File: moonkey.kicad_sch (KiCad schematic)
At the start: 35 parts, among them SW1 SW_Push, SW10 SW_Push, SW11 SW_Push, SW12 SW_Push, SW13 SW_Push, SW14 SW_Push, SW15 SW_Push, SW16 SW_Push, SW17 SW_Push, SW2 SW_Push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

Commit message: update
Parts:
- added J1: AudioJack4, moonkey:PJ320A, symbol Connector:AudioJack4
- RZ1: renamed from RZ?; footprint (none) -> moonkey:RP2040
- SW1, SW10, SW11, SW12, SW13, SW14, SW15, SW16, SW17, SW2, SW3, SW4, SW5, SW6, SW7, SW8, SW9: footprint Switch_Keyboard_Cherry_MX:SW_Cherry_MX_PCB_1.00u -> moonkey:Cherry_1u_rev
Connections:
- net COL0: now reaches D1.1 (K), D10.1 (K), D14.1 (K), D4.1 (K)
- net COL0: now also D7.1 (K), RZ1.17 (GP26)
- net ROW4: now reaches SW14.2, SW15.2, SW16.2, SW17.2
- net ROW4: now also RZ1.8 (GP7)
- net COL2: now reaches D12.1 (K), D16.1 (K), D3.1 (K), D6.1 (K), D9.1 (K)
- net COL2: now also RZ1.19 (GP28)
- net ROW0: now reaches SW1.2, SW2.2, SW3.2
- net ROW0: now also RZ1.1 (GP0)
- net ROW2: now reaches SW7.2, SW8.2, SW9.2
- net ROW2: now also RZ1.7 (GP6)
- net COL1: now reaches RZ1.18 (GP27)
- net COL1: now also D11.1 (K), D15.1 (K), D2.1 (K), D5.1 (K), D8.1 (K)
- net ROW1: now reaches RZ1.2 (GP1)
- net ROW1: now also SW4.2, SW5.2, SW6.2
- net COL3: now reaches RZ1.20 (GP29)
- net COL3: now also D13.1 (K), D17.1 (K)
- net +5V: now reaches RZ1.22 (5V)
- net +5V: now also J1.S
- net Earth: now reaches RZ1.23 (GND)
- net Earth: now also J1.T
- net SPI0_TX: now reaches RZ1.4 (GP3)
- net SPI0_TX: now also J1.R1
- net SPI0_RX: now reaches RZ1.5 (GP4)
- net SPI0_RX: now also J1.R2
- net ROW3: now reaches RZ1.9 (GP8)
- net ROW3: now also SW10.2, SW11.2, SW12.2, SW13.2
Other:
- moved on the sheet: D1, D10, D11, D12, D13, D14, D15, D16, D17, D2, D3, D4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

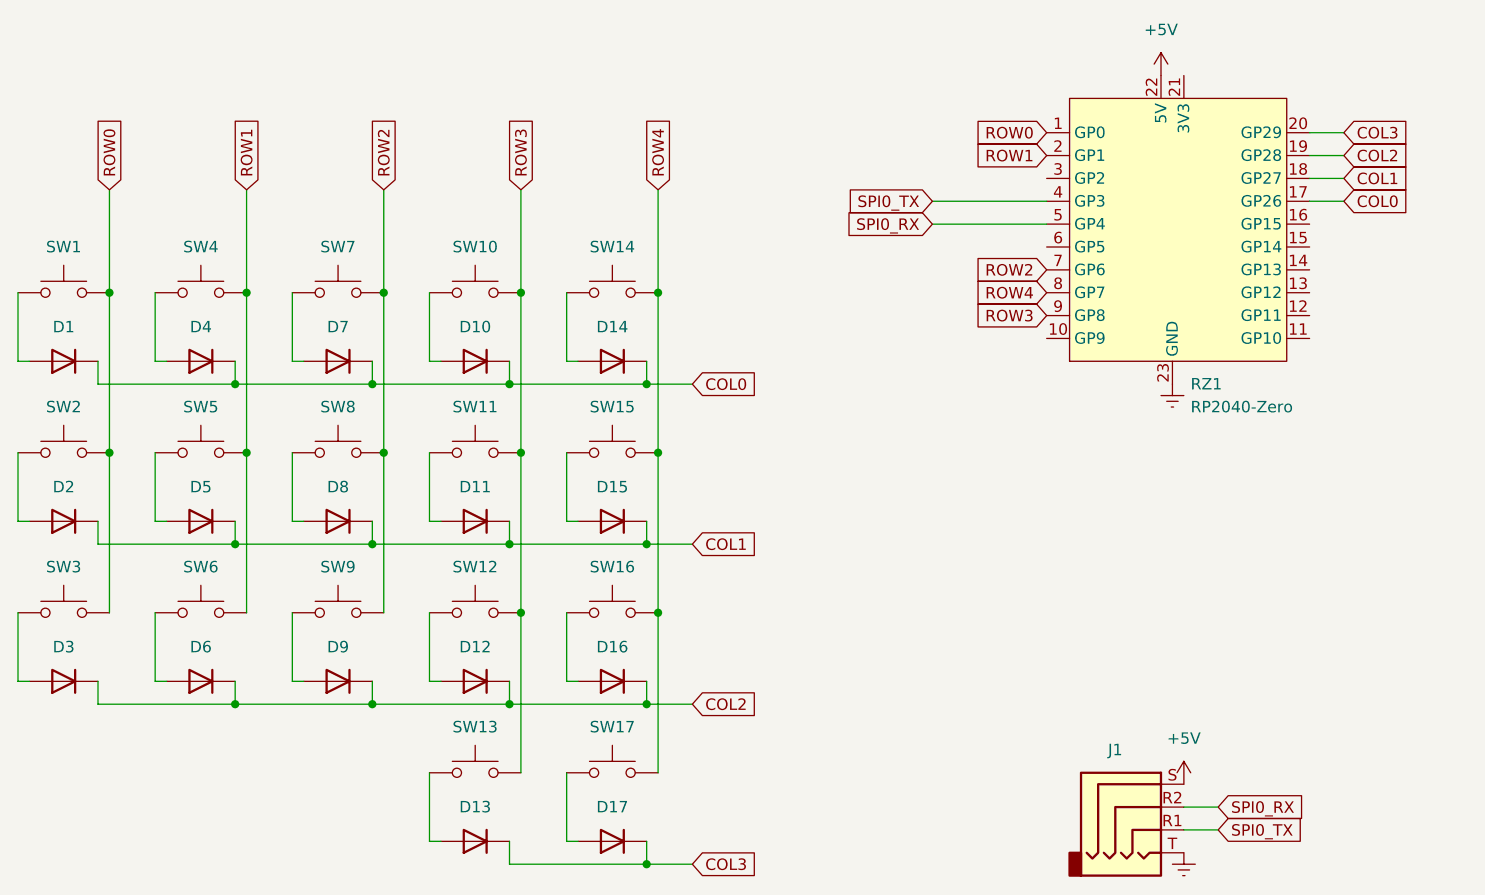
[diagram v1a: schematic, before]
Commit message: keyboard layout chagned, scheme update(pins change)
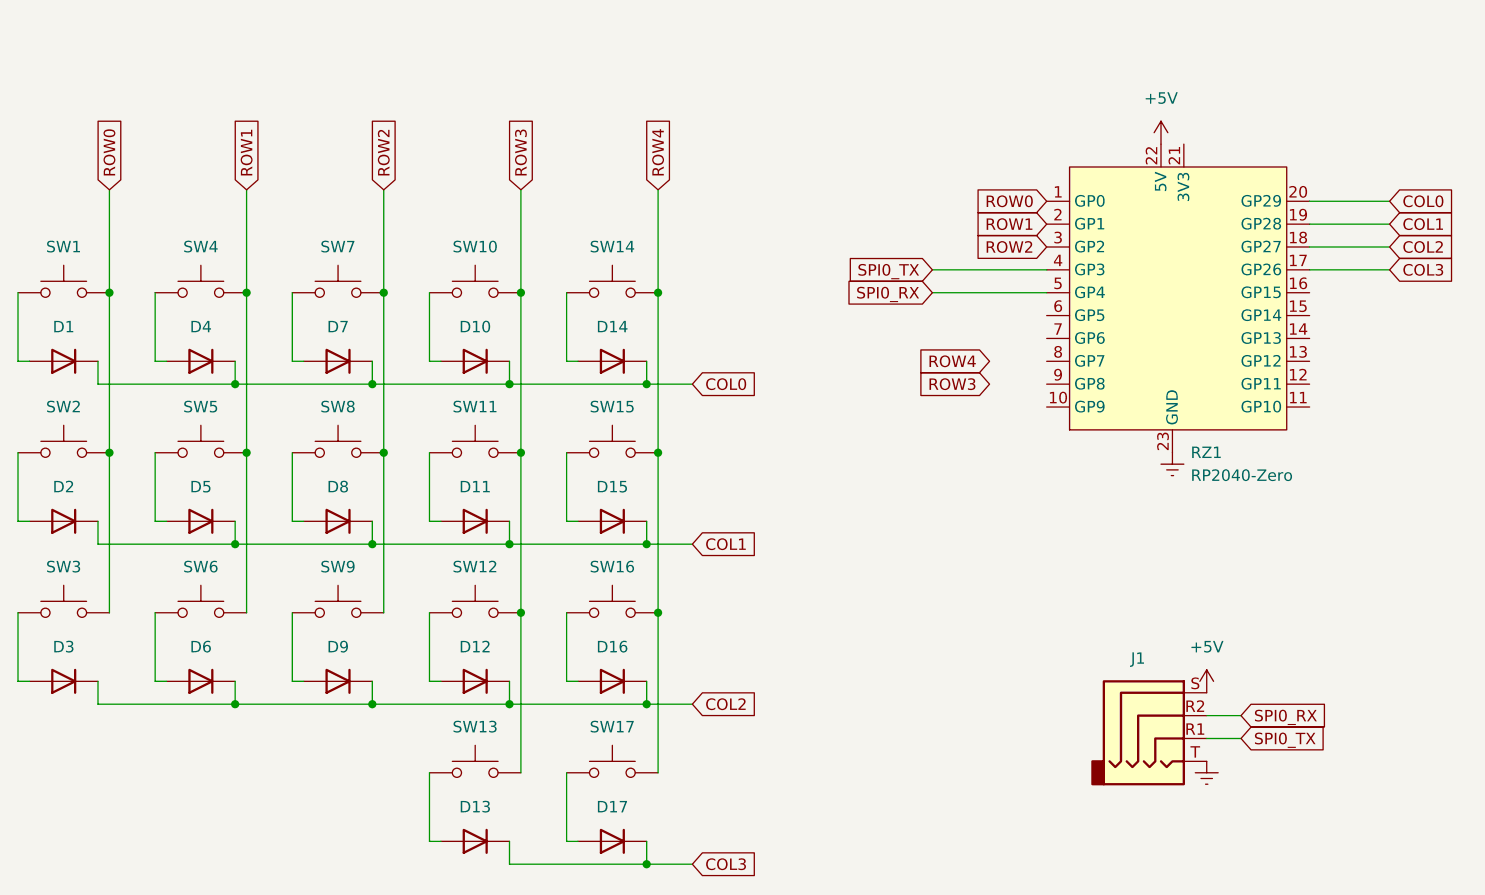
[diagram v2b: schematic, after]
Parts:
- J1: footprint moonkey:PJ320A -> moonkey:PJ320D_rev
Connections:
- net COL0: now also RZ1.20 (GP29); no longer RZ1.17 (GP26)
- net COL1: now also RZ1.19 (GP28); no longer RZ1.18 (GP27)
- net COL2: now also RZ1.18 (GP27); no longer RZ1.19 (GP28)
- net COL3: now also RZ1.17 (GP26); no longer RZ1.20 (GP29)
- net ROW2: now also RZ1.3 (GP2); no longer RZ1.7 (GP6)
- net ROW3: no longer RZ1.9 (GP8)
- net ROW4: no longer RZ1.8 (GP7)
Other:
- moved on the sheet: J1, RZ1

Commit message: uptate: ortholinear
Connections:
- net ROW3: now also RZ1.7 (GP6)
- net ROW4: now also RZ1.8 (GP7)
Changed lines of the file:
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@@
+    (stroke (width 0) (type default) (color 0 0 0 0))
+  )
+  (wire (pts (xy 151.13 86.36) (xy 153.67 86.36))
     (stroke (width 0) (type default) (color 0 0 0 0))
   )
@@
     (stroke (width 0) (type default) (color 0 0 0 0))
   )
+  (wire (pts (xy 151.13 71.12) (xy 153.67 71.12))
+    (stroke (width 0) (type default) (color 0 0 0 0))
+  )
   (wire (pts (xy 54.61 106.68) (xy 55.88 106.68))
     (stroke (width 0) (type default) (color 0 0 0 0))
@@
     (stroke (width 0) (type default) (color 0 0 0 0))
   )
+  (wire (pts (xy 151.13 73.66) (xy 153.67 73.66))
+    (stroke (width 0) (type default) (color 0 0 0 0))
+  )
   (wire (pts (xy 54.61 81.28) (xy 54.61 88.9))
     (stroke (width 0) (type default) (color 0 0 0 0))
@@
     (stroke (width 0) (type default) (color 0 0 0 0))
   )
+  (wire (pts (xy 151.13 88.9) (xy 153.67 88.9))
+    (stroke (width 0) (type default) (color 0 0 0 0))
+  )
   (wire (pts (xy 48.26 124.46) (xy 48.26 127))
     (stroke (width 0) (type default) (color 0 0 0 0))
@@
     (stroke (width 0) (type default) (color 0 0 0 0))
   )
+  (wire (pts (xy 151.13 76.2) (xy 153.67 76.2))
+    (stroke (width 0) (type default) (color 0 0 0 0))
+  )
   (wire (pts (xy 109.22 127) (xy 114.3 127))
     (stroke (width 0) (type default) (color 0 0 0 0))
@@
     )
   )
-  (global_label "ROW0" (shape input) (at 153.67 71.12 180) (fields_autoplaced)
-    (effects (font (size 1.27 1.27)) (justify right))
-    (property "시트 간 참조" "${INTERSHEET_REFS}" (id 0) (at 145.9955 71.0406 0)
+  (global_label "ROW0" (shape input) (at 151.13 71.12 180) (fields_autoplaced)
+    (effects (font (size 1.27 1.27)) (justify right))
+    (property "시트 간 참조" "${INTERSHEET_REFS}" (id 0) (at 143.4555 71.0406 0)
       (effects (font (size 1.27 1.27)) (justify right) hide)
     )
@@
     )
   )
-  (global_label "ROW1" (shape input) (at 153.67 73.66 180) (fields_autoplaced)
-    (effects (font (size 1.27 1.27)) (justify right))
-    (property "시트 간 참조" "${INTERSHEET_REFS}" (id 0) (at 145.9955 73.5806 0)
+  (global_label "ROW1" (shape input) (at 151.13 73.66 180) (fields_autoplaced)
+    (effects (font (size 1.27 1.27)) (justify right))
+    (property "시트 간 참조" "${INTERSHEET_REFS}" (id 0) (at 143.4555 73.5806 0)
       (effects (font (size 1.27 1.27)) (justify right) hide)
     )
@@
     )
   )
-  (global_label "ROW3" (shape input) (at 147.32 91.44 180) (fields_autoplaced)
-    (effects (font (size 1.27 1.27)) (justify right))
-    (property "시트 간 참조" "${INTERSHEET_REFS}" (id 0) (at 139.6455 91.3606 0)
+  (global_label "ROW3" (shape input) (at 151.13 86.36 180) (fields_autoplaced)
+    (effects (font (size 1.27 1.27)) (justify right))
+    (property "시트 간 참조" "${INTERSHEET_REFS}" (id 0) (at 143.4555 86.2806 0)
       (effects (font (size 1.27 1.27)) (justify right) hide)
     )
@@
     )
   )
-  (global_label "ROW2" (shape input) (at 153.67 76.2 180) (fields_autoplaced)
-    (effects (font (size 1.27 1.27)) (justify right))
-    (property "시트 간 참조" "${INTERSHEET_REFS}" (id 0) (at 145.9955 76.1206 0)
+  (global_label "ROW2" (shape input) (at 151.13 76.2 180) (fields_autoplaced)
+    (effects (font (size 1.27 1.27)) (justify right))
+    (property "시트 간 참조" "${INTERSHEET_REFS}" (id 0) (at 143.4555 76.1206 0)
       (effects (font (size 1.27 1.27)) (justify right) hide)
     )
@@
     )
   )
-  (global_label "ROW4" (shape input) (at 147.32 88.9 180) (fields_autoplaced)
-    (effects (font (size 1.27 1.27)) (justify right))
-    (property "시트 간 참조" "${INTERSHEET_REFS}" (id 0) (at 139.6455 88.8206 0)
-      (effects (font (size 1.27 1.27)) (justify right) hide)
-    )
+  (global_label "ROW4" (shape input) (at 151.13 88.9 180) (fields_autoplaced)
+    (effects (font (size 1.27 1.27)) (justify right))
+    (property "시트 간 참조" "${INTERSHEET_REFS}" (id 0) (at 143.4555 88.8206 0)
+      (effects (font (size 1.27 1.27)) (justify right) hide)
+    )
